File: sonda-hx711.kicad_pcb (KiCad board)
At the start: 2 copper layers, 53 parts, among them IC1 ATMEGA328P-A, J1 CONN_01X05, J2 CONN_01X02, J3 CONN_01X02, Q1 BC559, Q2 BC559, SW1 Reset, U1 AP1117-50, U10 HX711, U2 AP1117-33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

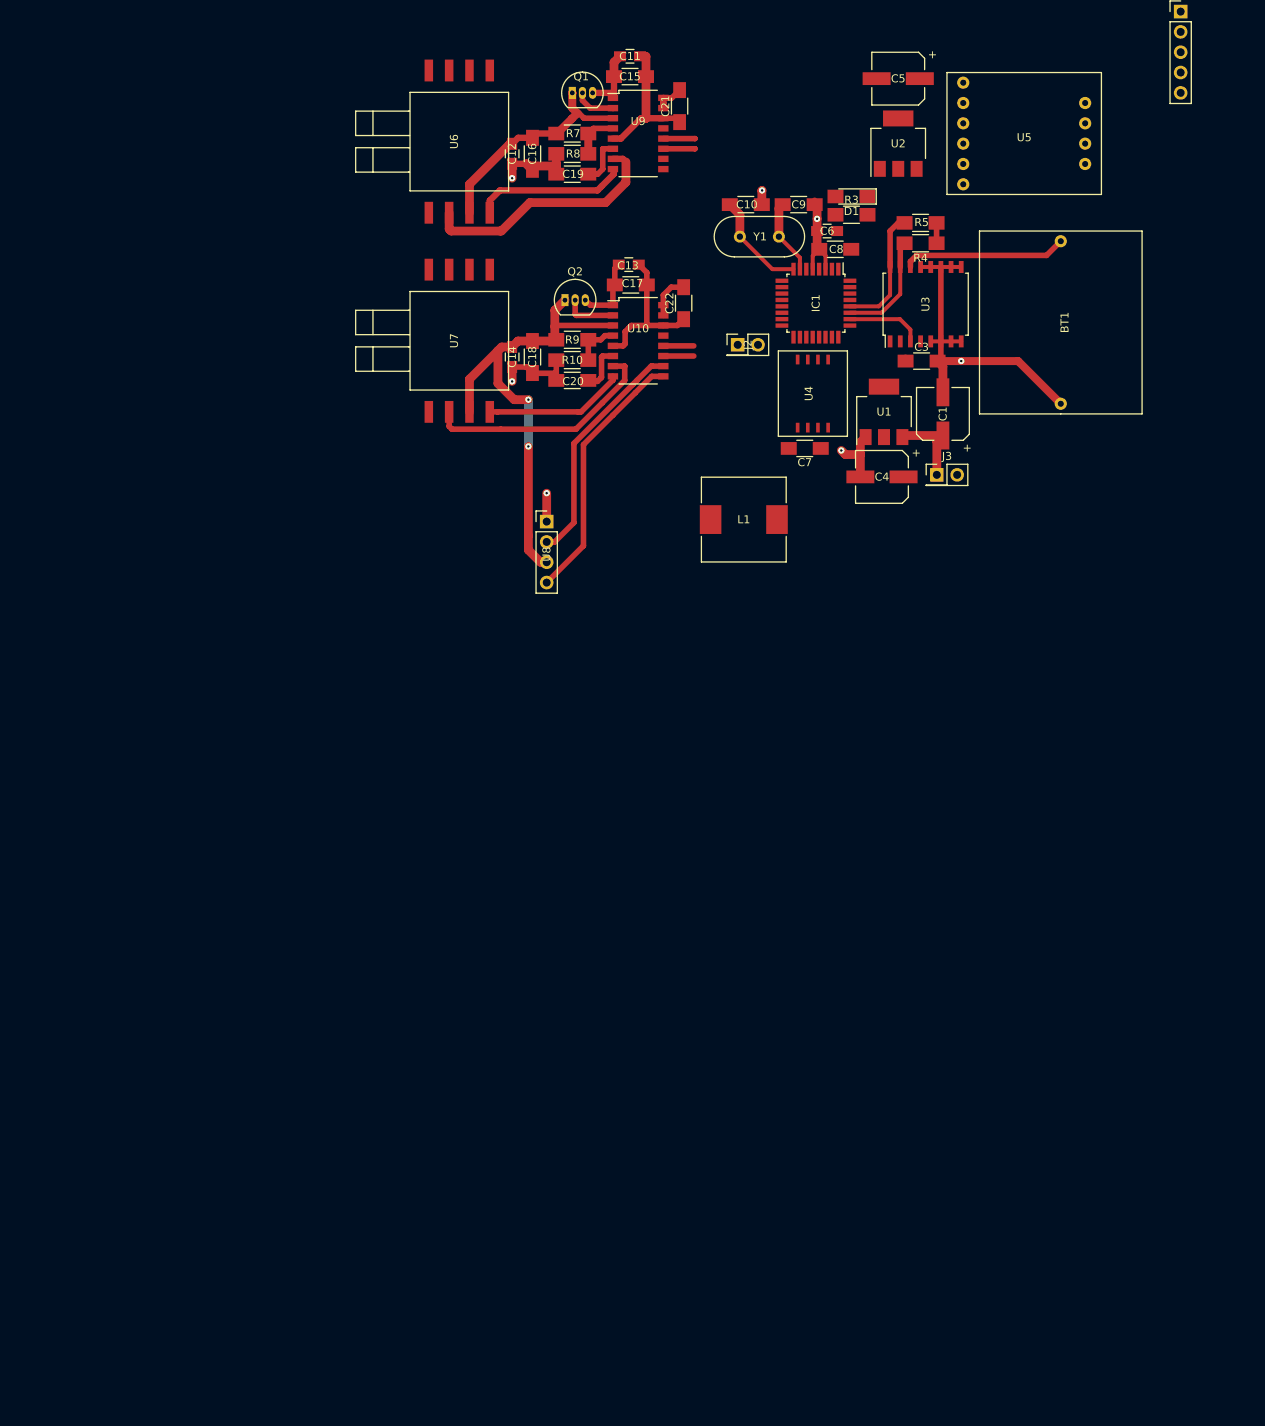
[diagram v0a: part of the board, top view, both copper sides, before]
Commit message: Updated MPX10 footprint.
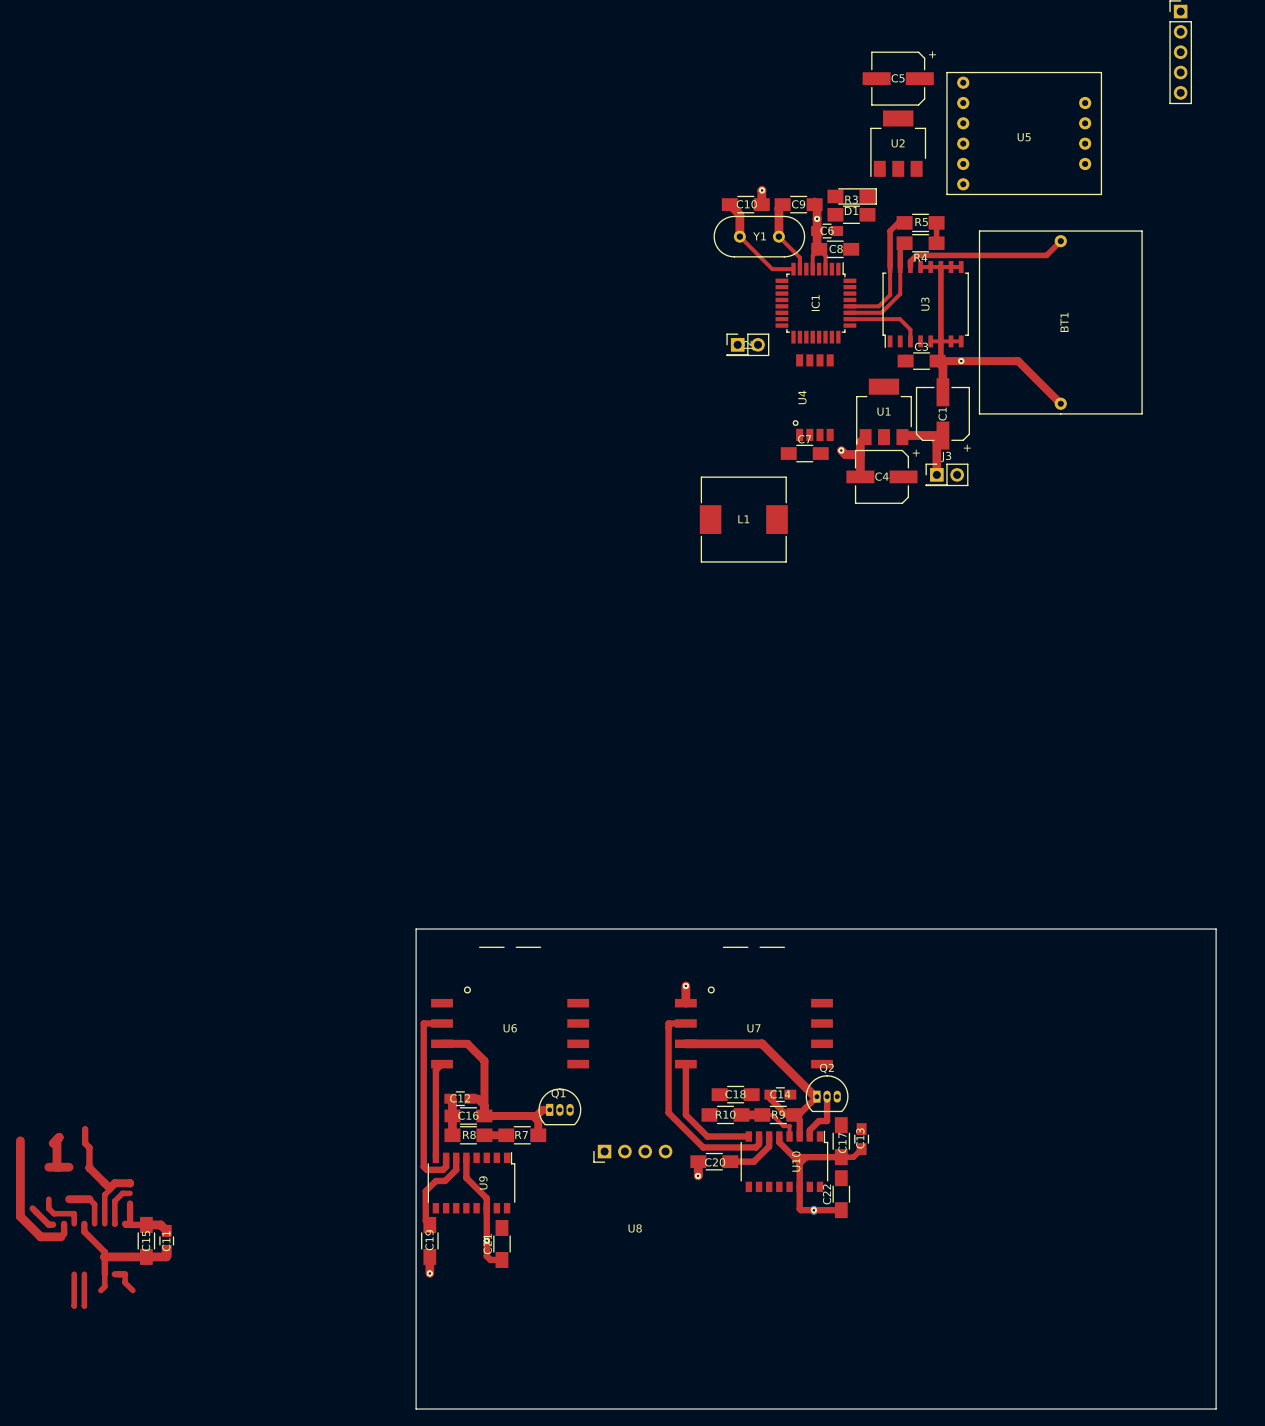
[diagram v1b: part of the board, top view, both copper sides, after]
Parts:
- U8: footprint Pin_Headers:Pin_Header_Straight_1x04_Pitch2.54mm -> custom-footprints:Freescale_Case_344C-01-IssueB-Unibody
- moved C11 159.0 mm to (-11.2, 174.0), turned to 90 degrees
- moved C15 157.6 mm to (-13.7, 174.0), turned to 90 degrees
- moved C21 144.0 mm to (30.7, 174.4)
- moved C19 134.5 mm to (21.7, 174.0), turned to 270 degrees
- moved U9 132.8 mm to (26.9, 166.8), turned to 270 degrees
- moved Q1 127.2 mm to (36.7, 157.6)
- moved R7 125.4 mm to (33.3, 160.8), turned to 180 degrees
- moved R8 123.4 mm to (26.5, 160.8)
- moved C16 120.5 mm to (26.5, 158.4), turned to 0 degrees
- moved C12 118.3 mm to (25.5, 156.2), turned to 0 degrees
- moved C13 113.1 mm to (75.7, 161.3), turned to 90 degrees
- moved C22 113.1 mm to (73.2, 168.1)
- moved U6 111.7 mm to (31.8, 148.1), turned to 180 degrees
- moved C17 110.2 mm to (73.1, 161.5), turned to 90 degrees
- moved Q2 104.4 mm to (70.1, 156.0)
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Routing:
- net (no net): track 0.00 -> 74.1 mm
- net /beta-Vout-: track 32.7 -> 0.00 mm
- net /alpha-beta-Vs: track 61.4 -> 30.2 mm, vias 2 -> 0
- net /beta-Vout+: track 29.5 -> 0.00 mm
- net +5V: track 28.0 -> 10.0 mm
- net Net-(U6-Pad4): track 18.9 -> 12.0 mm
- net Net-(U6-Pad2): track 31.1 -> 24.4 mm
- net GND: track 128.1 -> 134.6 mm, vias 7 -> 9
- net Net-(Q1-Pad2): track 5.16 -> 0.00 mm
- net Net-(C19-Pad1): track 5.88 -> 10.8 mm
- net /qbar_data: track 3.96 -> 0.00 mm
- net /qbar_clk: track 3.96 -> 0.00 mm
- net /angles_data: track 3.81 -> 0.00 mm
- net /angles_clk: track 3.81 -> 0.00 mm
- net Net-(R7-Pad2): track 5.89 -> 2.73 mm
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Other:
- board outline added: 100 x 60 mm

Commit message: Working on board layout.
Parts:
- added J4: CONN_01X04, Pin_Headers:Pin_Header_Straight_1x04_Pitch2.54mm, F.Cu at (104.3, 172.7)
- C1, C4, C5: footprint Capacitors_SMD:CP_Elec_6.3x5.3 -> Capacitors_ThroughHole:CP_Radial_Tantal_D4.5mm_P2.50mm
- moved R2 185.3 mm to (94.2, 158.2), turned to 270 degrees
- moved R1 181.4 mm to (96.8, 158.2), turned to 90 degrees
- moved U5 149.9 mm to (111.8, 184.7), turned to 90 degrees
- moved R5 124.7 mm to (168.0, 138.0)
- moved R4 124.7 mm to (168.0, 140.6)
- moved U3 113.0 mm to (113.8, 165.9)
- moved C3 113.0 mm to (113.2, 173.0)
- moved U1 110.3 mm to (95.5, 179.3), turned to 180 degrees
- moved C4 108.4 mm to (93.0, 185.9), turned to 0 degrees
- moved C1 104.1 mm to (99.8, 173.7)
- moved U4 99.9 mm to (88.9, 166.6), turned to 0 degrees
- moved L1 97.3 mm to (85.3, 178.1), turned to 90 degrees
- moved J2 97.0 mm to (81.6, 156.6), turned to 270 degrees
- moved D1 96.3 mm to (92.6, 138.0)
- moved R3 96.3 mm to (92.6, 140.3)
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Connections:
- IC1 pad 10: /qbar_clk -> /angles_clk
- IC1 pad 11: /angles_data -> /qbar_data
- IC1 pad 12: /angles_clk -> /qbar_clk
- IC1 pad 19: /BATT_MON -> Net-(IC1-Pad19)
- IC1 pad 23: Net-(IC1-Pad23) -> /PSTAT
- IC1 pad 24: /PSTAT -> /BATT_MON
- IC1 pad 9: /qbar_data -> /angles_data
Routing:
- net /TX: track 0.00 -> 95.7 mm, vias 0 -> 1
- net (no net): track 74.1 -> 0.00 mm
- net /qbar_clk: track 0.00 -> 67.6 mm
- net /qbar_data: track 0.00 -> 67.5 mm
- net GND: track 134.6 -> 82.9 mm, vias 9 -> 11
- net /angles_clk: track 0.00 -> 43.5 mm
- net /angles_data: track 0.00 -> 42.1 mm
- net /alpha-beta-Vs: track 30.2 -> 53.3 mm, vias 0 -> 1
- net Net-(BT1-Pad1): track 20.5 -> 0.00 mm
- net /beta-Vout+: track 0.00 -> 20.3 mm
- net Net-(Q1-Pad2): track 0.00 -> 13.1 mm
- net /beta-Vout-: track 0.00 -> 12.8 mm
- net /PSTAT: track 0.00 -> 11.7 mm
- net +BATT: track 10.4 -> 0.00 mm
- net /RTC_INT: track 9.58 -> 0.00 mm
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- added copper zone on F.Cu, net +5VA
- added copper zone on B.Cu, net GND
